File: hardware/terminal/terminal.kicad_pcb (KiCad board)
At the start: 2 copper layers, 14 parts, among them IC1 ATMEGA8-P, J1 RJ45, P1 Prog, P2 RC522, P3 LCD, P4 Keypad, U1 7805, U2 MAX232, U3 7803

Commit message: o (test; place programming header)
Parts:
- moved P1 25.6 mm to (77.7, 47.0), turned to 180 degrees
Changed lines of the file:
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@@
     (links 61)
     (no_connects 61)
-    (area 0 0 0 0)
+    (area 51.054 50.292 109.2914 82.212728)
     (thickness 1.6)
     (drawings 0)
@@
   )
   (module Connect:SIL-5 (layer F.Cu)
-    (at 80.160401 72.444018)
+    (at 77.724 46.99 180)
     (descr "Connecteur 5 pins")
     (tags "CONN DEV")
-    (fp_text reference P1 (at -0.635 -2.54) (layer F.SilkS)
+    (fp_text reference P1 (at -0.635 -2.54 180) (layer F.SilkS)
       (effects (font (size 1.72974 1.08712) (thickness 0.3048)))
     )
-    (fp_text value Prog (at 0 -2.54) (layer F.SilkS) hide
+    (fp_text value Prog (at 0 -2.54 180) (layer F.SilkS) hide
       (effects (font (size 1.524 1.016) (thickness 0.3048)))
     )
@@
     (fp_line (start 5.08 1.27) (end -7.62 1.27) (layer F.SilkS) (width 0.3048))
     (fp_line (start -5.08 1.27) (end -5.08 -1.27) (layer F.SilkS) (width 0.3048))
-    (pad 1 thru_hole rect (at -6.35 0) (size 1.397 1.397) (drill 0.8128) (layers *.Cu *.Mask F.SilkS)
+    (pad 1 thru_hole rect (at -6.35 0 180) (size 1.397 1.397) (drill 0.8128) (layers *.Cu *.Mask F.SilkS)
       (net 20 "Net-(IC1-Pad1)"))
-    (pad 2 thru_hole circle (at -3.81 0) (size 1.397 1.397) (drill 0.8128) (layers *.Cu *.Mask F.SilkS)
+    (pad 2 thru_hole circle (at -3.81 0 180) (size 1.397 1.397) (drill 0.8128) (layers *.Cu *.Mask F.SilkS)
       (net 23 MOSI))
-    (pad 3 thru_hole circle (at -1.27 0) (size 1.397 1.397) (drill 0.8128) (layers *.Cu *.Mask F.SilkS)
+    (pad 3 thru_hole circle (at -1.27 0 180) (size 1.397 1.397) (drill 0.8128) (layers *.Cu *.Mask F.SilkS)
       (net 24 MISO))
-    (pad 4 thru_hole circle (at 1.27 0) (size 1.397 1.397) (drill 0.8128) (layers *.Cu *.Mask F.SilkS)
+    (pad 4 thru_hole circle (at 1.27 0 180) (size 1.397 1.397) (drill 0.8128) (layers *.Cu *.Mask F.SilkS)
       (net 25 SCK))
-    (pad 5 thru_hole circle (at 3.81 0) (size 1.397 1.397) (drill 0.8128) (layers *.Cu *.Mask F.SilkS)
-      (net 5 GND))
-  )
+    (pad 5 thru_hole circle (at 3.81 0 180) (size 1.397 1.397) (drill 0.8128) (layers *.Cu *.Mask F.SilkS)
+      (net 5 GND))
+  )

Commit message: o Basic placement.
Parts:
- moved C4 106.0 mm to (158.2, 68.8), turned to 90 degrees
- moved P4 94.4 mm to (152.0, 46.0), turned to 270 degrees
- moved C2 94.3 mm to (154.8, 73.8), turned to 180 degrees
- moved C1 93.8 mm to (150.5, 73.8), turned to 180 degrees
- moved U1 85.9 mm to (173.5, 52.0)
- moved C3 85.8 mm to (149.5, 68.2), turned to 90 degrees
- moved U3 81.6 mm to (175.0, 40.5)
- moved U2 79.3 mm to (154.0, 68.2)
- moved R1 77.1 mm to (122.2, 43.0)
- moved IC1 70.5 mm to (141.0, 55.0), turned to 90 degrees
- moved J1 69.9 mm to (171.0, 65.5), turned to 90 degrees
- moved P2 60.6 mm to (121.5, 55.2), turned to 90 degrees
- moved P1 49.1 mm to (126.0, 38.0)
- moved P3 46.8 mm to (129.5, 64.5), turned to 270 degrees
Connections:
- net Net-(J1-Pad3) renamed /TX-ext
- net Net-(J1-Pad6) renamed /RX-ext
- P4 pad 1: KROW-0 -> Net-(P4-Pad1)
- P4 pad 11: KCOL-1 -> KROW-2
- P4 pad 13: KCOL-2 -> KROW-1
- P4 pad 15: Net-(P4-Pad15) -> KROW-0
- P4 pad 3: KROW-1 -> KCOL-2
- P4 pad 5: KROW-2 -> KCOL-1
- P4 pad 7: KROW-3 -> KCOL-0
- P4 pad 9: KCOL-0 -> KROW-3
- R1 pad 2: Net-(R1-Pad2) -> Net-(IC1-Pad16)
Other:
- board outline added: 60 x 40 mm

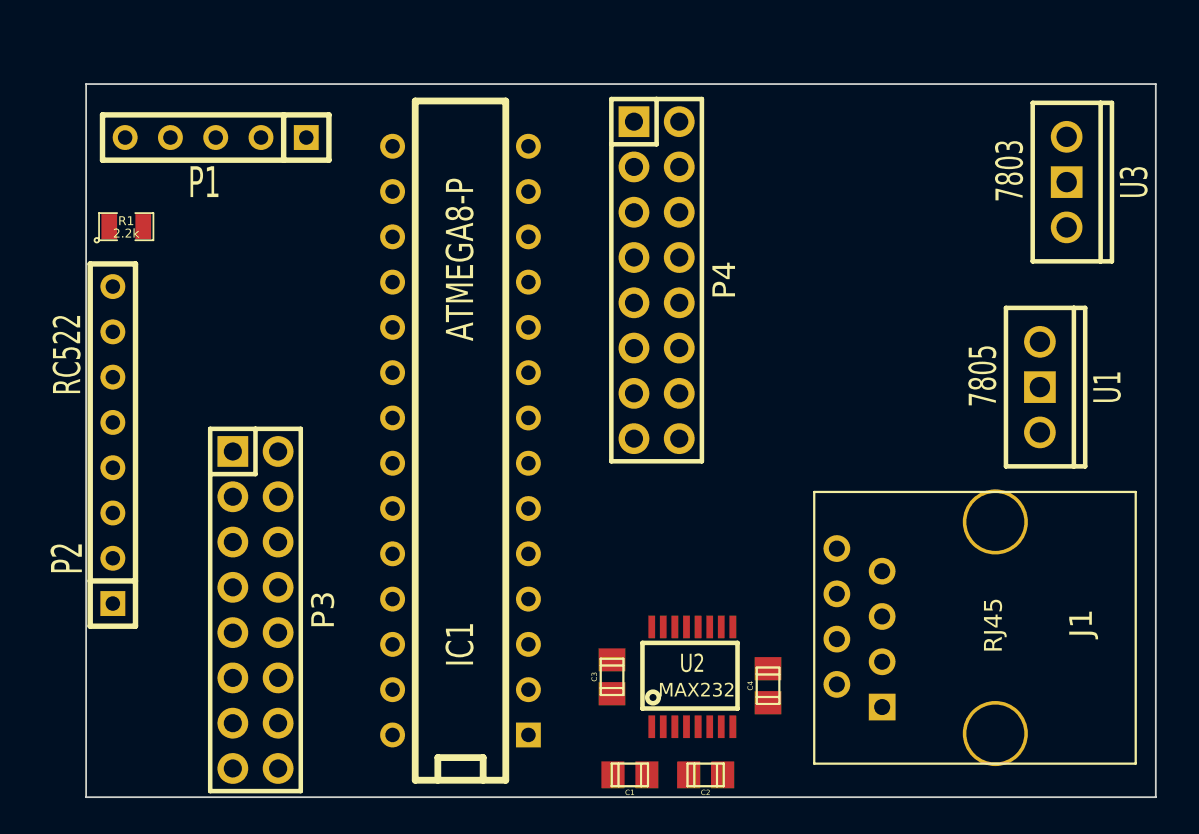
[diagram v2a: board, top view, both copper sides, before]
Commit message: Work in progress  o more layout work done  o use chargepump of remaining rs232 driver to provide negative    voltage to display.
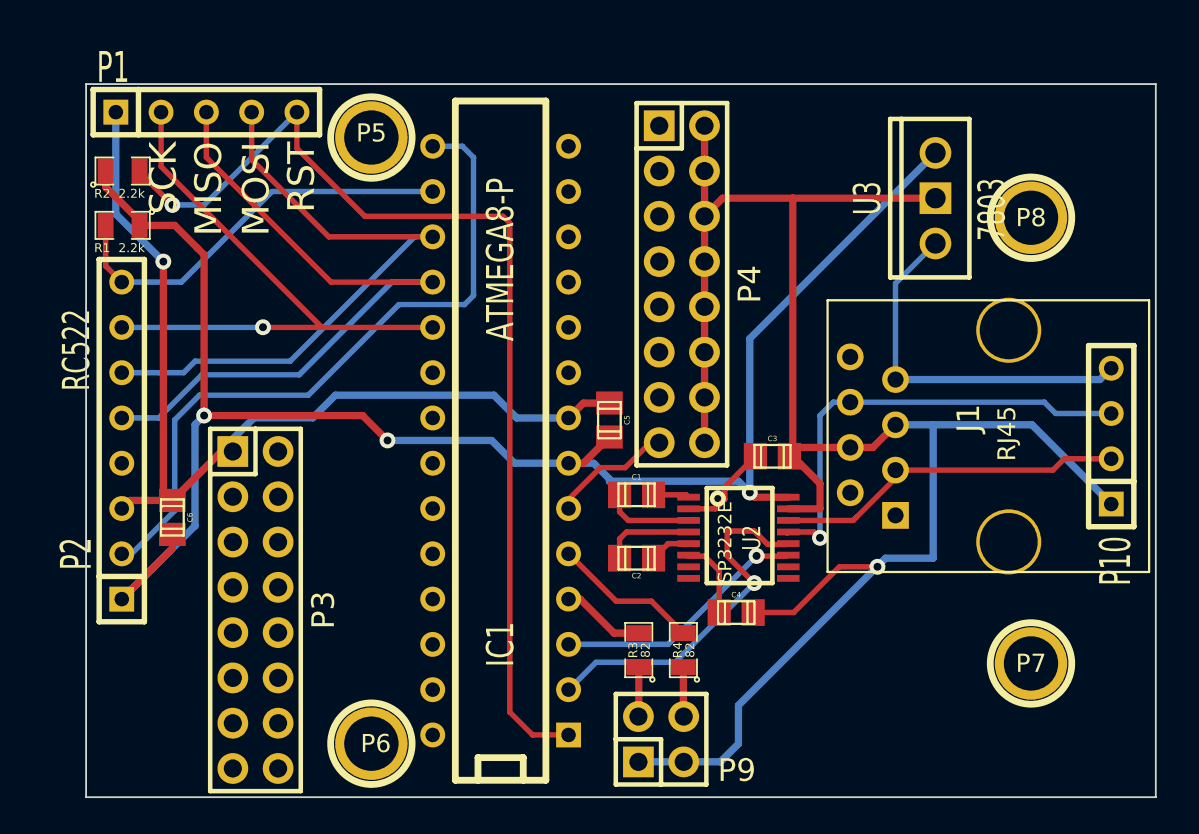
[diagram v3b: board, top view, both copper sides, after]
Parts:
- removed U1: 7805, Discret:LM78XXV
- added C5: C, Capacitors_SMD:c_0805, F.Cu at (149.4, 53.8)
- added C6: C, Capacitors_SMD:c_0805, F.Cu at (124.8, 59.3)
- added P10: CONN_4, Connect:SIL-4, F.Cu at (177.5, 54.8)
- added P5: CONN_1, Connect:1pin, F.Cu at (136.0, 38.0)
- added P6: CONN_1, Connect:1pin, F.Cu at (136.0, 72.0)
- added P7: CONN_1, Connect:1pin, F.Cu at (173.0, 67.5)
- added P8: CONN_1, Connect:1pin, F.Cu at (173.0, 42.5)
- added P9: CONN_2X2, Pin_Headers:Pin_Header_Straight_2x02, F.Cu at (152.2, 71.8)
- added R2: 2.2k, SMD_Packages:SM0805, F.Cu at (122.0, 39.9)
- added R3: 82, SMD_Packages:SM0805, F.Cu at (151.0, 66.8)
- added R4: 82, SMD_Packages:SM0805, F.Cu at (153.5, 66.8)
- U2: value MAX232 -> SP3232E
- moved C1 15.7 mm to (150.9, 58.0), turned to 0 degrees
- moved C3 15.3 mm to (158.5, 55.9), turned to 0 degrees
- moved C2 12.8 mm to (150.9, 61.6)
- moved J1 10.8 mm to (171.8, 54.8)
- moved U2 8.22 mm to (156.6, 60.5), turned to 270 degrees
- moved U3 7.42 mm to (167.6, 41.4), turned to 180 degrees
- moved C4 4.48 mm to (156.5, 64.6), turned to 0 degrees
- moved P1 2.47 mm to (128.0, 36.6), turned to 0 degrees
- moved IC1 2.25 mm to (143.2, 55.0)
- moved P4 1.43 mm to (153.4, 46.2)
- moved P2 0.56 mm to (122.0, 55.0)
- moved R1 0.22 mm to (122.0, 42.9), turned to 180 degrees
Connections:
- net /RX-ext renamed RX-ext
- net /TX-ext renamed TX-ext
- net Net-(IC1-Pad15) renamed /RST-RFID
- net Net-(IC1-Pad16) renamed /CS-RFID
- P1 pad 1: Net-(IC1-Pad1) -> GND
- P1 pad 2: MOSI -> SCK
- P1 pad 4: SCK -> MOSI
- P1 pad 5: GND -> Net-(IC1-Pad1)
- P3 pad 3: GND -> LCD-contr
- U2 pad 10: GND -> +3.3V
- U2 pad 7: Net-(U2-Pad7) -> LCD-contr
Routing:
- net GND: track 0.00 -> 165.0 mm, vias 0 -> 2
- net +3.3V: track 0.00 -> 95.2 mm, vias 0 -> 3
- net Net-(IC1-Pad1): track 0.00 -> 58.8 mm, vias 0 -> 1
- net /RST-RFID: track 0.00 -> 39.0 mm
- net MISO: track 0.00 -> 38.7 mm
- net MOSI: track 0.00 -> 35.2 mm
- net SCK: track 0.00 -> 33.3 mm, vias 0 -> 1
- net RX-ext: track 0.00 -> 25.7 mm, vias 0 -> 1
- net /CS-RFID: track 0.00 -> 23.2 mm
- net +12V: track 0.00 -> 20.9 mm
- net RX: track 0.00 -> 20.1 mm, vias 0 -> 1
- net TX-ext: track 0.00 -> 19.8 mm
- net TX: track 0.00 -> 14.3 mm, vias 0 -> 1
- net Net-(IC1-Pad5): track 0.00 -> 8.71 mm
- net KROW-0: track 0.00 -> 6.91 mm
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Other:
- net class Default: trace_width 0.254 -> 0.3048
- net class power added: clearance 0.2032, trace_width 0.4064, via_dia 0.889, via_drill 0.635
- net class thin added: clearance 0.254, trace_width 0.254, via_dia 0.889, via_drill 0.635
- board text added: "MISO"
- board text added: "MOSI"
- board text added: "RST"
- board text added: "SCK"

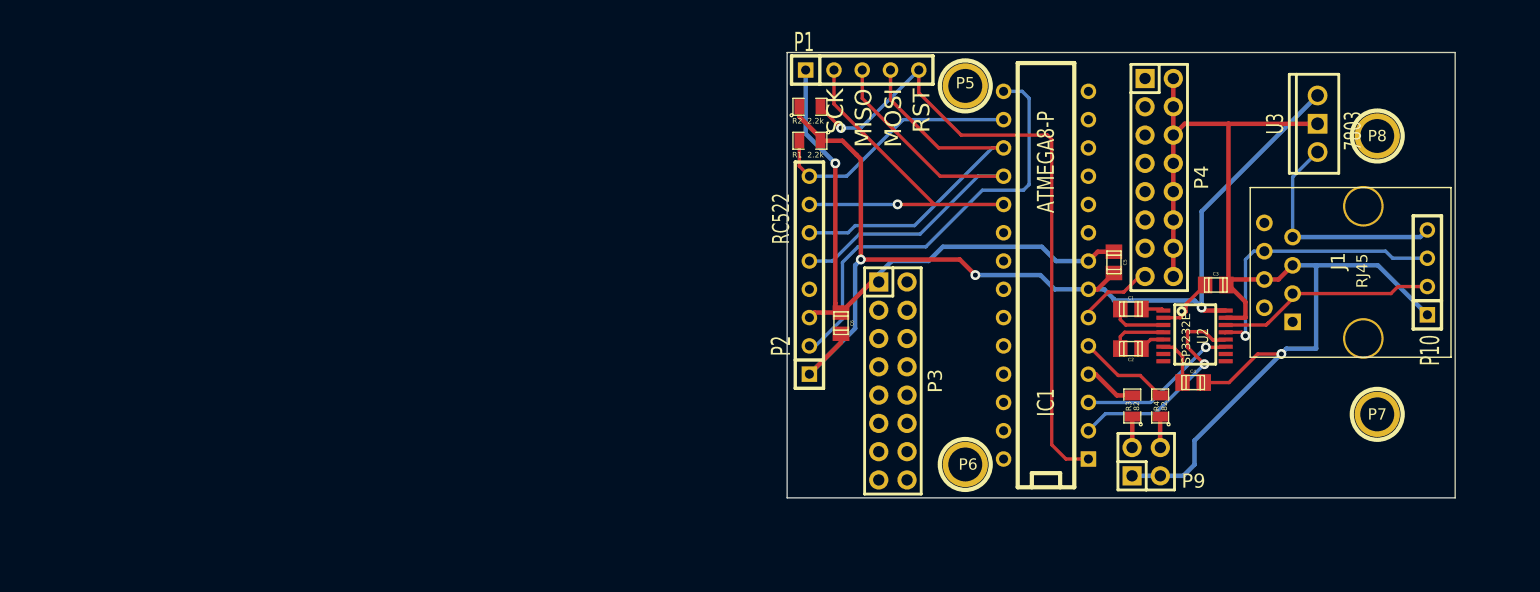
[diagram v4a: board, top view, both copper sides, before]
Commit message: o First complete routing. o Add voltage divider to get a proper negative voltage for LCD.
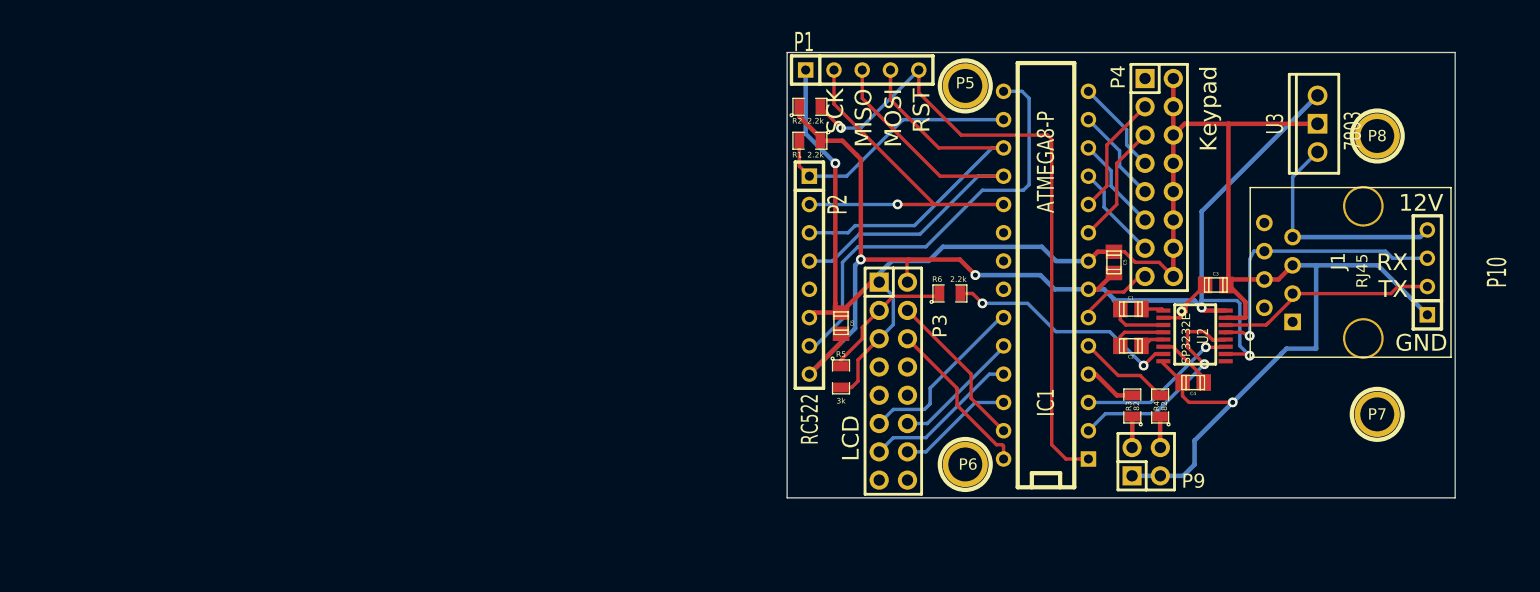
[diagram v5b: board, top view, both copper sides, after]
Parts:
- added R5: 3k, SMD_Packages:SMD-0805, F.Cu at (124.8, 64.1)
- added R6: 2.2k, SMD_Packages:SMD-0805, F.Cu at (134.6, 56.6)
- moved C2 0.25 mm to (150.9, 61.3)
- turned C4 to 180 degrees
- turned P2 to 270 degrees
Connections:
- P2 pad 1: +3.3V -> /CS-RFID
- P2 pad 2: /RST-RFID -> SCK
- P2 pad 3: GND -> MOSI
- P2 pad 4: Net-(P2-Pad4) -> MISO
- P2 pad 5: MISO -> Net-(P2-Pad5)
- P2 pad 6: MOSI -> GND
- P2 pad 7: SCK -> /RST-RFID
- P2 pad 8: /CS-RFID -> +3.3V
- P3 pad 2: +5V -> +3.3V
- P3 pad 3: LCD-contr -> Net-(P3-Pad3)
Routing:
- net LCD-contr: track 0.00 -> 21.3 mm, vias 0 -> 2
- net GND: track 165.0 -> 184.2 mm
- net LCD-D0: track 0.00 -> 15.9 mm
- net LCD-EN: track 0.00 -> 14.7 mm
- net LCD-RS: track 0.00 -> 14.4 mm
- net LCD-D2: track 0.00 -> 14.1 mm
- net +3.3V: track 95.2 -> 108.2 mm, vias 3 -> 4
- net Net-(P3-Pad3): track 0.00 -> 12.5 mm
- net LCD-D1: track 0.00 -> 11.6 mm
- net KCOL-1: track 0.00 -> 10.9 mm
- net KCOL-2: track 0.00 -> 10.9 mm
- net LCD-D3: track 0.00 -> 10.5 mm
- net KROW-1: track 0.00 -> 8.57 mm
- net KROW-3: track 0.00 -> 8.57 mm
- net KROW-2: track 0.00 -> 8.57 mm
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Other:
- net class Default: clearance 0.254 -> 0.2032
- rule trace_clearance: 0.254 -> 0.2032
- board text added: "12V"
- board text added: "GND"
- board text added: "Keypad"
- board text added: "LCD"
- board text added: "RX"
- board text added: "TX"

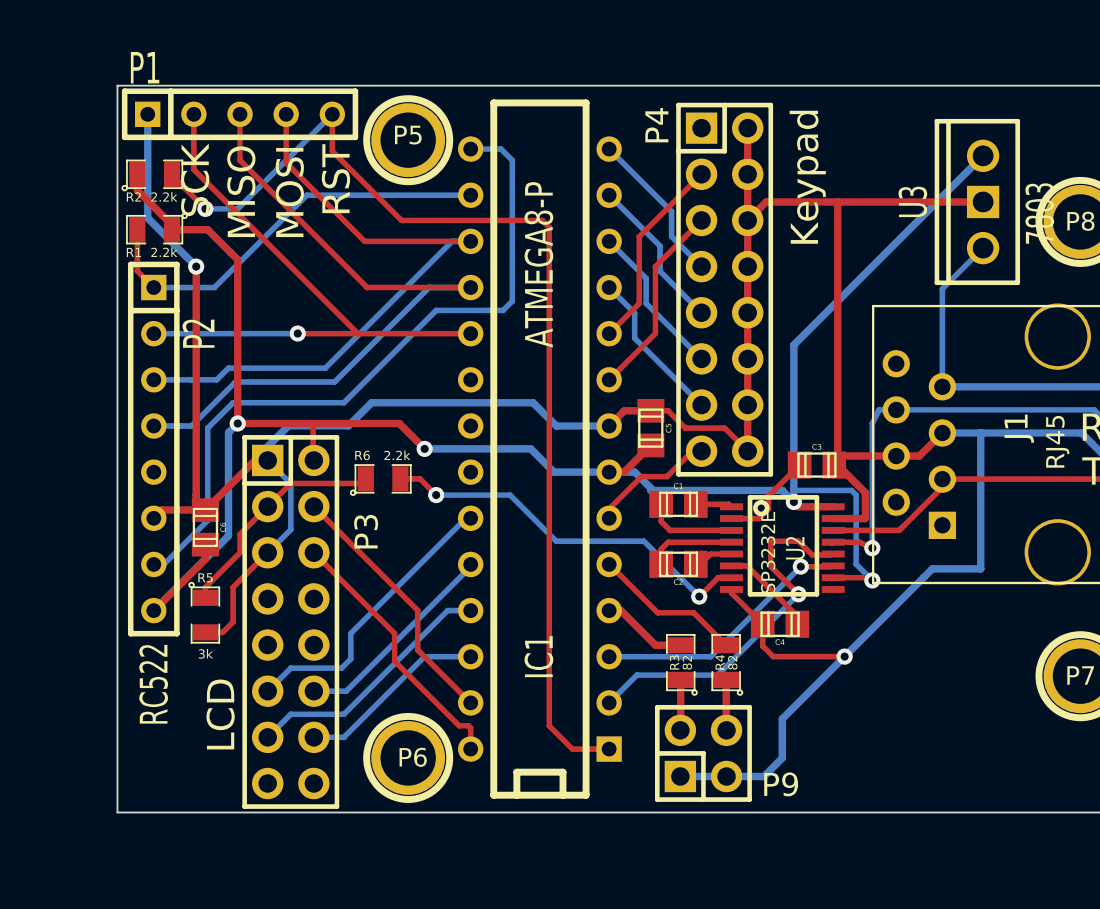
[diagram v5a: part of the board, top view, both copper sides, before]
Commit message: o Move programming header inwards a bit so that it doesn't   collicde with chrystal
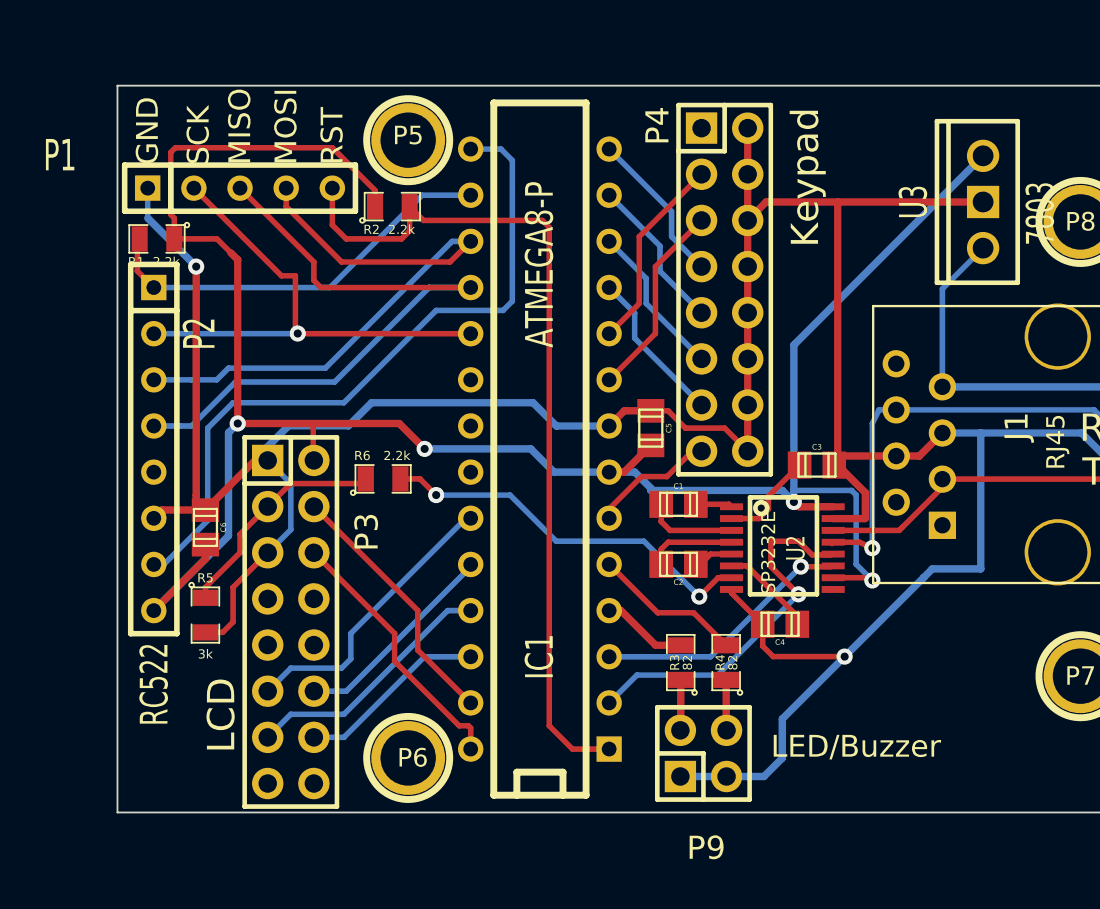
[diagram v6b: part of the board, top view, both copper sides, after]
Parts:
- moved R2 13.2 mm to (135.1, 41.7)
- moved P1 4.06 mm to (128.0, 40.6)
- moved R1 0.52 mm to (122.2, 43.4)
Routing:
- net +3.3V: track 108.2 -> 122.1 mm
- net Net-(IC1-Pad1): track 58.8 -> 47.5 mm, vias 1 -> 0
- net SCK: track 33.3 -> 28.3 mm
- net GND: track 184.2 -> 180.2 mm
- net MISO: track 38.7 -> 36.2 mm
- net MOSI: track 35.2 -> 33.5 mm
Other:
- board text added: "LED/Buzzer"
